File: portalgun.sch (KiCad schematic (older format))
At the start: 35 parts, among them J1 Conn_01x02_Male, J2 Rotary Encoder / Switch Header, J3 Conn_01x02_Male, J4 Conn_01x02_Male, J5 Conn_02x03_Odd_Even, J7 Conn_01x04_Male, J8 Conn_01x04_Male, Q1 MMBT3904, U1 NCP1421, U3 NCP4589DSN33T1G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

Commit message: Main Board Rev A files
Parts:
- removed C12, C14: 1uF, Capacitor_SMD:C_0603_1608Metric, symbol Device:C
- removed C8, C?: 10uF, Capacitor_Tantalum_SMD:CP_EIA-2012-15_AVX-P, symbol Device:CP
- removed J2: Rotary Encoder / Switch Header, Connector_PinHeader_2.00mm:PinHeader_1x05_P2.00mm_Vertical, symbol Connector:Conn_01x05_Male
- removed J5: Conn_02x03_Odd_Even, Connector_PinHeader_2.54mm:PinHeader_1x06_P2.54mm_Horizontal, symbol Connector_Generic:Conn_02x03_Odd_Even
- removed J7, J8: Conn_01x04_Male, Connector_PinHeader_2.00mm:PinHeader_1x04_P2.00mm_Vertical, symbol Connector:Conn_01x04_Male
- removed L?: L, symbol Device:L
- removed Q1: MMBT3904, Package_TO_SOT_SMD:SOT-23, symbol Transistor_BJT:MMBT3904
- removed R10, R11, R12, R9: 100, Resistor_SMD:R_0603_1608Metric_Pad0.98x0.95mm_HandSolder, symbol Device:R_Small
- removed R5, R6, R7: 10k, Resistor_SMD:R_0603_1608Metric_Pad0.98x0.95mm_HandSolder, symbol Device:R_Small
- removed U3: NCP4589DSN33T1G, Package_TO_SOT_SMD:SOT-23-5, symbol CustomPower:NCP4589DSN33T1G
- removed U4: STM32L011G4Ux, Package_DFN_QFN:QFN-28_4x4mm_P0.5mm, symbol MCU_ST_STM32L0:STM32L011G4Ux
- added C11: 10uF, Capacitor_Tantalum_SMD:CP_EIA-2012-15_AVX-P, symbol Device:CP
- added C2: 10uF, Capacitor_SMD:C_0805_2012Metric, symbol Device:C
- added C8, C9: 1uF, Capacitor_SMD:C_0603_1608Metric, symbol Device:C
- added J10, J5: Conn_01x02_Male, Connector_PinHeader_2.00mm:PinHeader_1x02_P2.00mm_Vertical, symbol Connector:Conn_01x02_Male
- added J2: Conn_01x07_Male, Connector_Molex:Molex_PicoBlade_53047-0710_1x07_P1.25mm_Vertical, symbol Connector:Conn_01x07_Male
- added J9: Conn_01x04_Female, Connector_Molex:Molex_PicoBlade_53047-0410_1x04_P1.25mm_Vertical, symbol Connector:Conn_01x04_Female
- added Q1, Q2, Q3: BS316N, Package_TO_SOT_SMD:SOT-23, symbol Device:Q_NMOS_GSD
- added R10, R11: 200, Resistor_SMD:R_0603_1608Metric, symbol Device:R
- added R15, R16, R6, R9: 10k, Resistor_SMD:R_0603_1608Metric, symbol Device:R
- added R5: 1k, Resistor_SMD:R_0603_1608Metric, symbol Device:R
- added SW1, SW2: SW_MEC_5E, Button_Switch_THT:SW_TH_Tactile_Omron_B3F-10xx, symbol Switch:SW_MEC_5E
- added U2: ESP-12F, RF_Module:ESP-12E, symbol RF_Module:ESP-12F
- added U3: MIC5504-3.3YM5, Package_TO_SOT_SMD:SOT-23-5, symbol Regulator_Linear:MIC5504-3.3YM5
- added U6, U7, U8: 74AHC1G125, Package_TO_SOT_SMD:SOT-353_SC-70-5, symbol 74xGxx:74AHC1G125
- R8: value 1k -> 200; footprint Resistor_SMD:R_0603_1608Metric_Pad0.98x0.95mm_HandSolder -> Resistor_SMD:R_0603_1608Metric
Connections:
- net labels added: ESP_RXD, ESP_TXD, I2S_BCLK, I2S_DATA, I2S_LRCLK, LED1, LED2, LED3, SCL, SDA, bootsel, ~DISPLAY_RST, ~rst
- net labels removed: ENCODER_A, ENCODER_B, I2C1_SCL, I2C1_SDA, LED_GATE, LPUART1_RX, LPUART1_TX, SWITCH, SYS_SWCLK, SYS_SWDIO, VDDA, enc_a, enc_b, enc_c, sw_a, sw_b
- wire segments 141 -> 191
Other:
- note added: "TODO:\nVerify I2C and I2S Pins\nReset and boot switches\nuser button"
- moved on the sheet: J3, J4

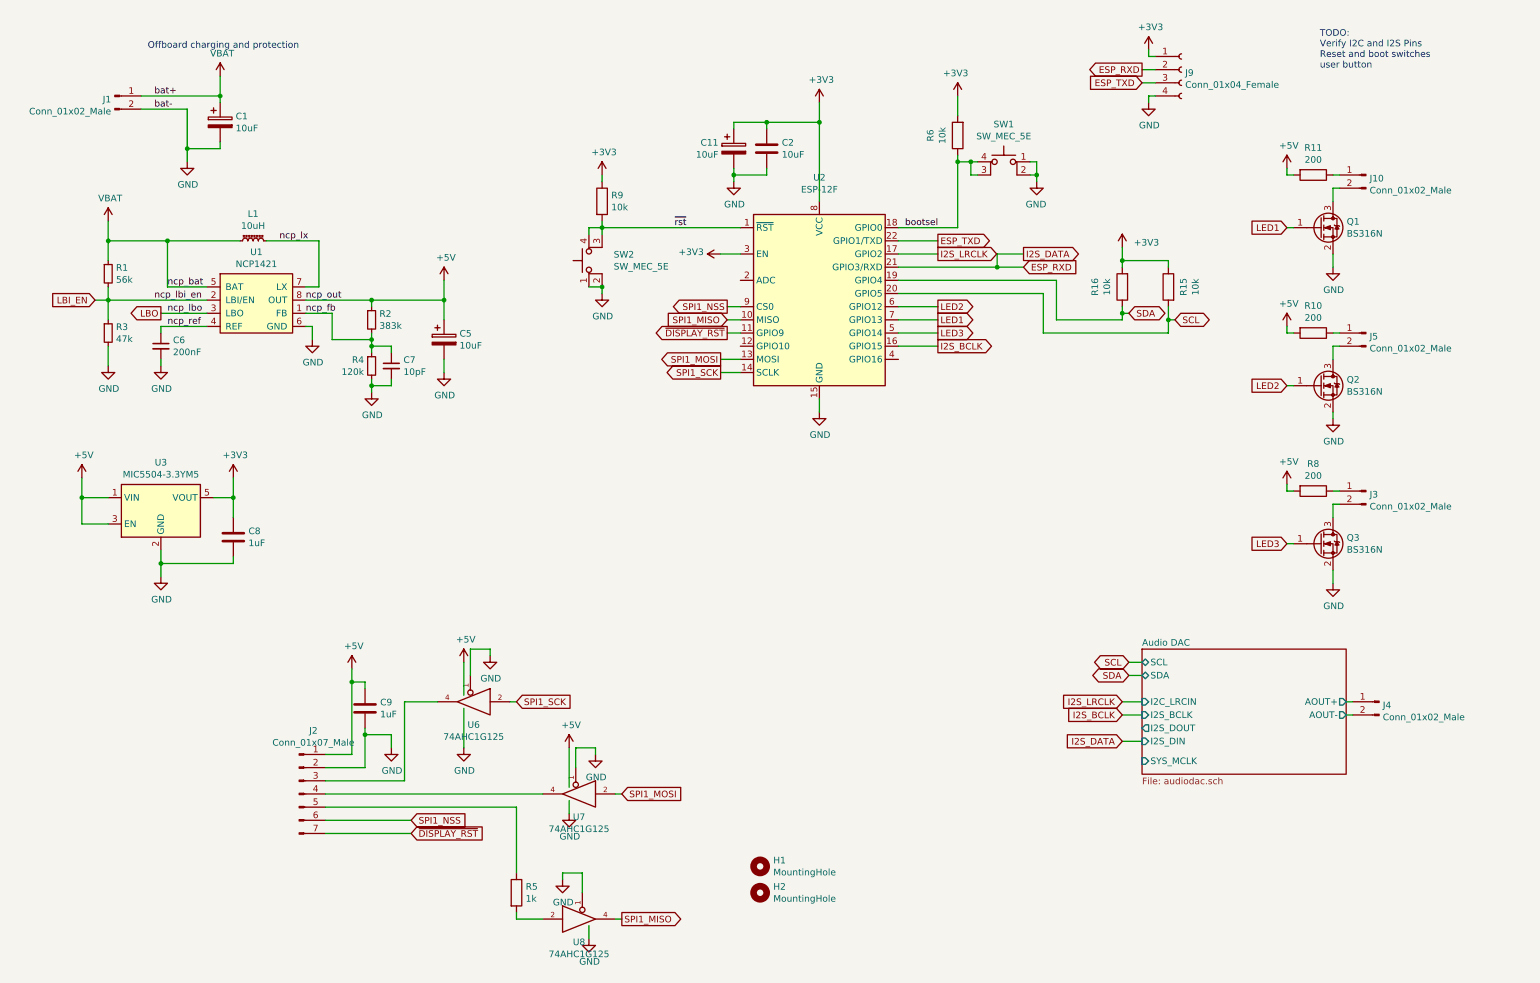
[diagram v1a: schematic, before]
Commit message: Rev B Portal Gun Mainboard as ordered
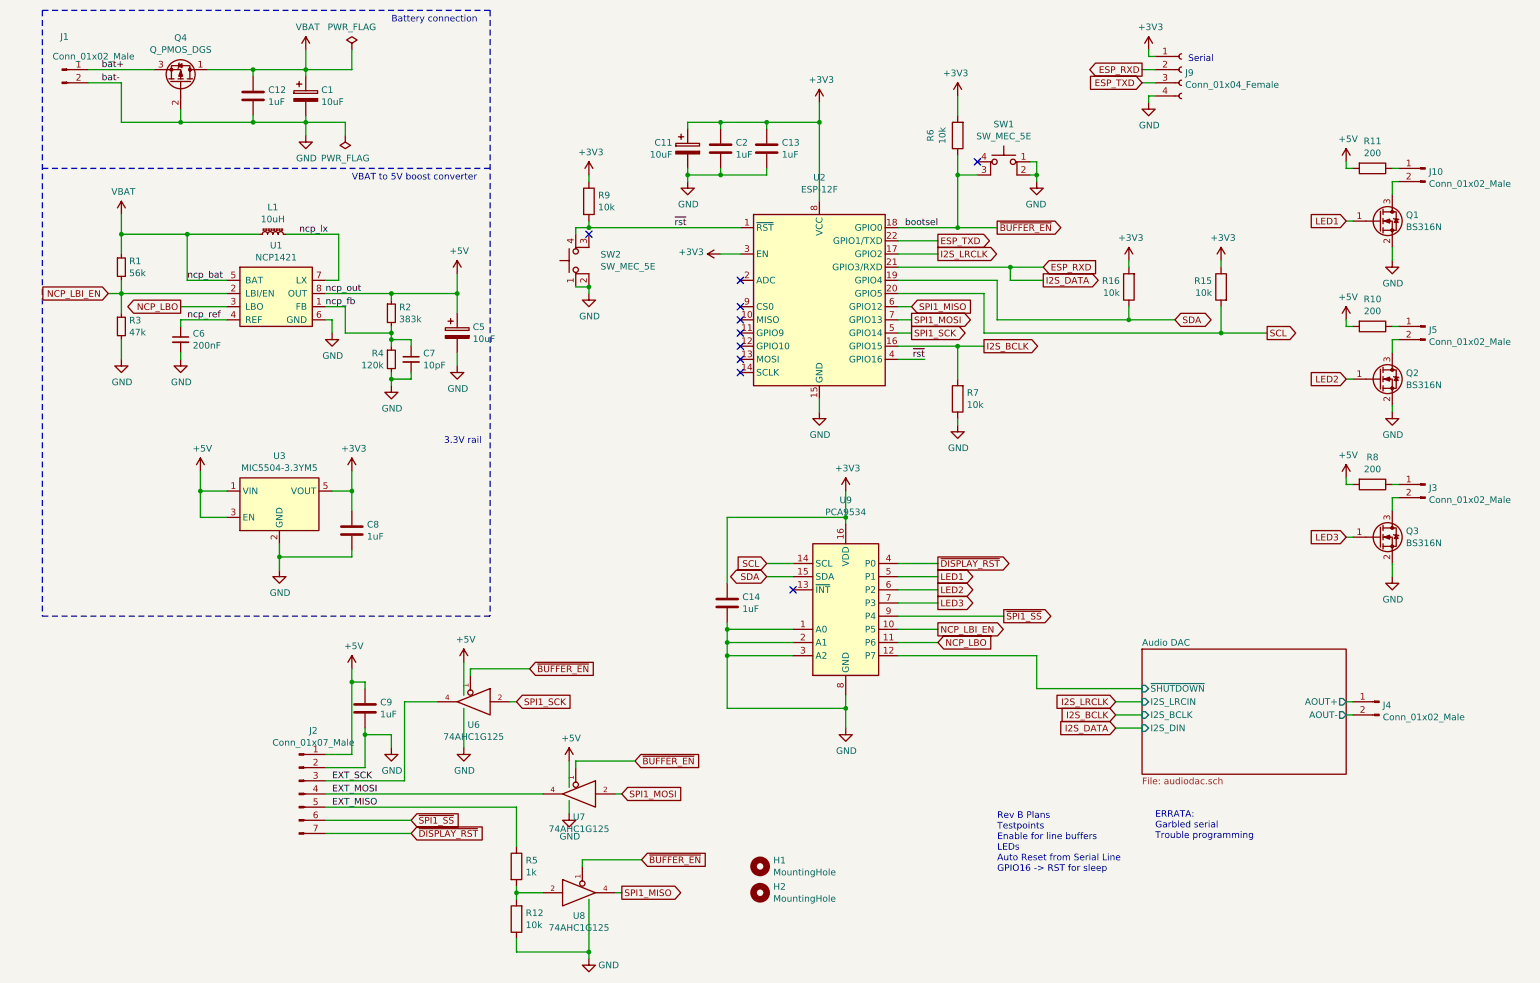
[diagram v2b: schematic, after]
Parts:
- added C12, C13, C14: 1uF, Capacitor_SMD:C_0805_2012Metric, symbol Device:C
- added Q4: Q_PMOS_DGS, Package_TO_SOT_SMD:SOT-23, symbol Device:Q_PMOS_DGS
- added R12, R7: 10k, Resistor_SMD:R_0603_1608Metric, symbol Device:R
- added U9: PCA9534, Package_SO:SSOP-16_5.3x6.2mm_P0.65mm, symbol Interface_Expansion:TCA9534
- C2: value 10uF -> 1uF
- C8, C9: footprint Capacitor_SMD:C_0603_1608Metric -> Capacitor_SMD:C_0805_2012Metric
- J1, J10, J3, J4, J5: footprint Connector_PinHeader_2.00mm:PinHeader_1x02_P2.00mm_Vertical -> Connector_PinHeader_2.54mm:PinHeader_1x02_P2.54mm_Vertical
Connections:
- net +3V3: now also C13.1, C14.1, U9.16 (VDD)
- net GND: now also C12.2, C13.2, C14.2, Q4.2 (G), R12.1, R7.1, U9.1 (A0), U9.2 (A1), U9.3 (A2), U9.8 (GND); no longer U6.1, U7.1, U8.1
- net I2S_BCLK: now also R7.2
- net LED1: now also U9.5 (P1); no longer U2.7 (GPIO13)
- net LED2: now also U9.6 (P2); no longer U2.6 (GPIO12)
- net LED3: now also U9.7 (P3); no longer U2.5 (GPIO14)
- net SCL: now also U9.14 (SCL)
- net SDA: now also U9.15 (SDA)
- net SPI1_MISO: now also U2.6 (GPIO12); no longer U2.10 (MISO)
- net SPI1_MOSI: now also U2.7 (GPIO13); no longer U2.13 (MOSI)
- net SPI1_SCK: now also U2.5 (GPIO14); no longer U2.14 (SCLK)
- net VBAT: now also C12.1, Q4.1 (D); no longer J1.1 (Pin_1)
- net ~DISPLAY_RST: now also U9.4 (P0); no longer U2.11 (GPIO9)
- net ~rst: now also U2.4 (GPIO16); no longer SW2.3 (K)
- net EXT_SCK: now reaches J2.3 (Pin_3), U6.4
- net EXT_MOSI: now reaches J2.4 (Pin_4), U7.4
- net EXT_MISO: now reaches J2.5 (Pin_5), R5.1
- net at R5.2, U8.2: now also R12.2
- net LBI_EN renamed NCP_LBI_EN
- net NCP_LBI_EN: now also U9.10 (P5)
- net LBO renamed NCP_LBO
- net NCP_LBO: now also U9.11 (P6)
- net SPI1_NSS: no longer names the net of U2.9 (CS0)
- net SPI1_NSS: no longer J2.6 (Pin_6)
- net bootsel renamed ~BUFFER_EN
- net ~BUFFER_EN: now also U6.1, U7.1, U8.1; no longer SW1.4 (A)
- new net Audio DAC/~SHUTDOWN: U9.12 (P7)
- new net bat+: J1.1 (Pin_1), Q4.3 (S)
- new net ~SPI1_SS: J2.6 (Pin_6), U9.9 (P4)
- no-connect marks 0 -> 10
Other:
- note added: "3.3V rail"
- note added: "Battery connection"
- note added: "ERRATA:\nGarbled serial\nTrouble programming"
- note added: "Rev B Plans\nTestpoints\nEnable for line buffers\nLEDs\nAuto Reset from Serial Line\nGPIO16 -> RST for sleep"
- note added: "Serial"
- note added: "VBAT to 5V boost converter"
- note removed: "Offboard charging and protection"
- note removed: "TODO:\nVerify I2C and I2S Pins\nReset and boot switches\nuser button"
- moved on the sheet: C1, C11, C2, C5, C6, C7, C8, J1, J10, J3, J5, L1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
